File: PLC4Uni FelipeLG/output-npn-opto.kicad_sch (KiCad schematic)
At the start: 3 parts

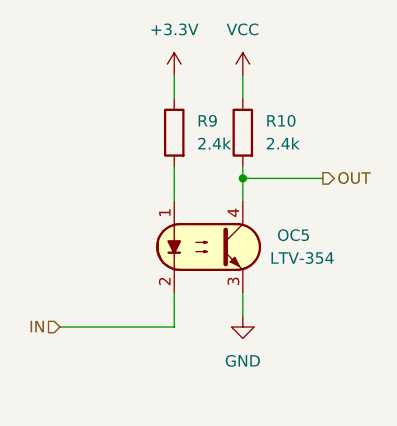
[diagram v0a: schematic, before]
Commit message: Add files via upload
Updated Circuitos corregidos y pistas agregadas
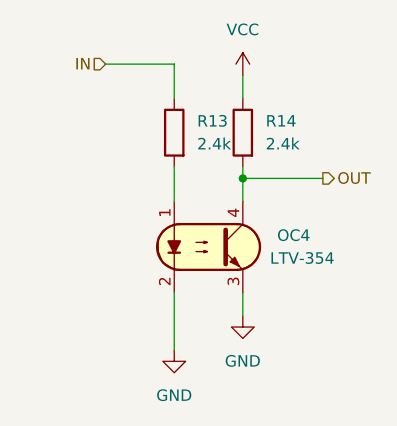
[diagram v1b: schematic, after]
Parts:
- renumbered OC5 to OC4, R9 to R13, R10 to R14
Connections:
- net +3.3V is gone; now on net IN: R13.2
- net GND: now also OC4.2
- net IN: no longer OC4.2
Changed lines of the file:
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@@
-	(wire
-		(pts
-			(xy 110.49 127) (xy 123.19 127)
-		)
-		(stroke
-			(width 0)
-			(type default)
-		)
-	)
 	(wire
 		(pts
@@
 	(wire
 		(pts
-			(xy 123.19 99.06) (xy 123.19 101.6)
+			(xy 123.19 97.79) (xy 123.19 101.6)
 		)
 		(stroke
@@
 	(wire
 		(pts
-			(xy 123.19 127) (xy 123.19 123.19)
+			(xy 123.19 123.19) (xy 123.19 129.54)
 		)
 		(stroke
@@
 		(pts
 			(xy 130.81 99.06) (xy 130.81 101.6)
+		)
+		(stroke
+			(width 0)
+			(type default)
+		)
+	)
+	(wire
+		(pts
+			(xy 115.57 97.79) (xy 123.19 97.79)
 		)
 		(stroke
@@
 	(hierarchical_label "IN"
 		(shape input)
-		(at 110.49 127 180)
+		(at 115.57 97.79 180)
 		(effects
 			(font
@@
 		(dnp no)
 		(fields_autoplaced yes)
-		(property "Reference" "R10"
+		(property "Reference" "R14"
 			(at 133.35 104.1399 0)
 			(effects
@@
 			(project "Diseños de circuitos"
 				(path "/65c875c0-73bd-43df-b6cd-4a685398cace/3b453a73-5bb7-4645-a7e8-6e186968fa05/304245ed-3772-43ea-9156-20acc62cd04b"
-					(reference "R12")
+					(reference "R20")
 					(unit 1)
 				)
 				(path "/65c875c0-73bd-43df-b6cd-4a685398cace/3b453a73-5bb7-4645-a7e8-6e186968fa05/51c169c5-6841-4f27-afaa-a4e6455b756e"
-					(reference "R10")
+					(reference "R14")
 					(unit 1)
 				)
@@
 		(on_board yes)
 		(dnp no)
-		(property "Reference" "OC5"
+		(property "Reference" "OC4"
 			(at 134.62 116.8399 0)
 			(effects
@@
 				)
 				(path "/65c875c0-73bd-43df-b6cd-4a685398cace/3b453a73-5bb7-4645-a7e8-6e186968fa05/51c169c5-6841-4f27-afaa-a4e6455b756e"
-					(reference "OC5")
-					(unit 1)
-				)
-			)
-		)
-	)
-	(symbol
-		(lib_id "power:+3.3V")
-		(at 123.19 99.06 0)
-		(unit 1)
-		(exclude_from_sim no)
-		(in_bom yes)
-		(on_board yes)
-		(dnp no)
-		(fields_autoplaced yes)
-		(property "Reference" "#PWR018"
-			(at 123.19 102.87 0)
-			(effects
-				(font
-					(size 1.27 1.27)
-				)
-				(hide yes)
-			)
-		)
-		(property "Value" "+3.3V"
-			(at 123.19 93.98 0)
-			(effects
-				(font
-					(size 1.27 1.27)
-				)
-			)
-		)
-		(property "Footprint" ""
-			(at 123.19 99.06 0)
-			(effects
-				(font
-					(size 1.27 1.27)
-				)
-				(hide yes)
-			)
-		)
-		(property "Datasheet" ""
-			(at 123.19 99.06 0)
-			(effects
-				(font
-					(size 1.27 1.27)
-				)
-				(hide yes)
-			)
-		)
-		(property "Description" "Power symbol creates a global label with name \"+3.3V\""
-			(at 123.19 99.06 0)
-			(effects
-				(font
-					(size 1.27 1.27)
-				)
-				(hide yes)
-			)
-		)
-		(pin "1"
-		)
-		(instances
-			(project "Diseños de circuitos"
-				(path "/65c875c0-73bd-43df-b6cd-4a685398cace/3b453a73-5bb7-4645-a7e8-6e186968fa05/304245ed-3772-43ea-9156-20acc62cd04b"
-					(reference "#PWR021")
-					(unit 1)
-				)
-				(path "/65c875c0-73bd-43df-b6cd-4a685398cace/3b453a73-5bb7-4645-a7e8-6e186968fa05/51c169c5-6841-4f27-afaa-a4e6455b756e"
-					(reference "#PWR018")
+					(reference "OC4")
 					(unit 1)
 				)
@@
 		(dnp no)
 		(fields_autoplaced yes)
-		(property "Reference" "#PWR019"
+		(property "Reference" "#PWR027"
 			(at 130.81 132.08 0)
 			(effects
@@
 			(project "Diseños de circuitos"
 				(path "/65c875c0-73bd-43df-b6cd-4a685398cace/3b453a73-5bb7-4645-a7e8-6e186968fa05/304245ed-3772-43ea-9156-20acc62cd04b"
-					(reference "#PWR022")
+					(reference "#PWR037")
 					(unit 1)
 				)
 				(path "/65c875c0-73bd-43df-b6cd-4a685398cace/3b453a73-5bb7-4645-a7e8-6e186968fa05/51c169c5-6841-4f27-afaa-a4e6455b756e"
-					(reference "#PWR019")
+					(reference "#PWR027")
 					(unit 1)
 				)
@@
 		(dnp no)
 		(fields_autoplaced yes)
-		(property "Reference" "#PWR017"
+		(property "Reference" "#PWR026"
 			(at 130.81 102.87 0)
 			(effects
@@
 			(project "Diseños de circuitos"
 				(path "/65c875c0-73bd-43df-b6cd-4a685398cace/3b453a73-5bb7-4645-a7e8-6e186968fa05/304245ed-3772-43ea-9156-20acc62cd04b"
-					(reference "#PWR020")
+					(reference "#PWR036")
 					(unit 1)
 				)
 				(path "/65c875c0-73bd-43df-b6cd-4a685398cace/3b453a73-5bb7-4645-a7e8-6e186968fa05/51c169c5-6841-4f27-afaa-a4e6455b756e"
-					(reference "#PWR017")
+					(reference "#PWR026")
 					(unit 1)
 				)
@@
 		(dnp no)
 		(fields_autoplaced yes)
-		(property "Reference" "R9"
+		(property "Reference" "R13"
 			(at 125.73 104.1399 0)
 			(effects
@@
 			(project "Diseños de circuitos"
 				(path "/65c875c0-73bd-43df-b6cd-4a685398cace/3b453a73-5bb7-4645-a7e8-6e186968fa05/304245ed-3772-43ea-9156-20acc62cd04b"
-					(reference "R11")
+					(reference "R19")
 					(unit 1)
 				)
 				(path "/65c875c0-73bd-43df-b6cd-4a685398cace/3b453a73-5bb7-4645-a7e8-6e186968fa05/51c169c5-6841-4f27-afaa-a4e6455b756e"
-					(reference "R9")
-					(unit 1)
-				)
+					(reference "R13")
+					(unit 1)
+				)
+			)
+		)
+	)
+	(symbol
+		(lib_id "power:GND")
+		(at 123.19 129.54 0)
+		(unit 1)
+		(exclude_from_sim no)
+		(in_bom yes)
+		(on_board yes)
+		(dnp no)
+		(fields_autoplaced yes)
+		(property "Reference" "#PWR025"
+			(at 123.19 135.89 0)
+			(effects
+				(font
+					(size 1.27 1.27)
+				)
+				(hide yes)
+			)
+		)
+		(property "Value" "GND"
+			(at 123.19 134.62 0)
+			(effects
+				(font
+					(size 1.27 1.27)
+				)
+			)
+		)
+		(property "Footprint" ""
+			(at 123.19 129.54 0)
+			(effects
+				(font
+					(size 1.27 1.27)
+				)
+				(hide yes)
+			)
+		)
+		(property "Datasheet" ""
+			(at 123.19 129.54 0)
+			(effects
+				(font
+					(size 1.27 1.27)
+				)
+				(hide yes)
+			)
+		)
+		(property "Description" "Power symbol creates a global label with name \"GND\" , ground"
+			(at 123.19 129.54 0)
+			(effects
+				(font
+					(size 1.27 1.27)
+				)
+				(hide yes)
+			)
+		)
+		(pin "1"
+		)
+		(instances
+			(project "PLC4Uni FelipeLG"
+				(path "/65c875c0-73bd-43df-b6cd-4a685398cace/3b453a73-5bb7-4645-a7e8-6e186968fa05/304245ed-3772-43ea-9156-20acc62cd04b"
+					(reference "#PWR035")
+					(unit 1)
+				)
+				(path "/65c875c0-73bd-43df-b6cd-4a685398cace/3b453a73-5bb7-4645-a7e8-6e186968fa05/51c169c5-6841-4f27-afaa-a4e6455b756e"
+					(reference "#PWR025")
+					(unit 1)
+				)
